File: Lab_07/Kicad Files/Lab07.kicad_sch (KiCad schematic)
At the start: 31 parts, among them J101 Conn_01x01_Socket, J102 Conn_01x01_Socket, J103 Conn_01x01_Socket, J104 Conn_01x01_Socket, J105 Conn_01x01_Pin, J106 Conn_01x01_Pin, J301 Conn_01x01_Socket, J302 Conn_01x01_Socket, J303 Conn_01x01_Socket, J304 Conn_01x01_Socket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

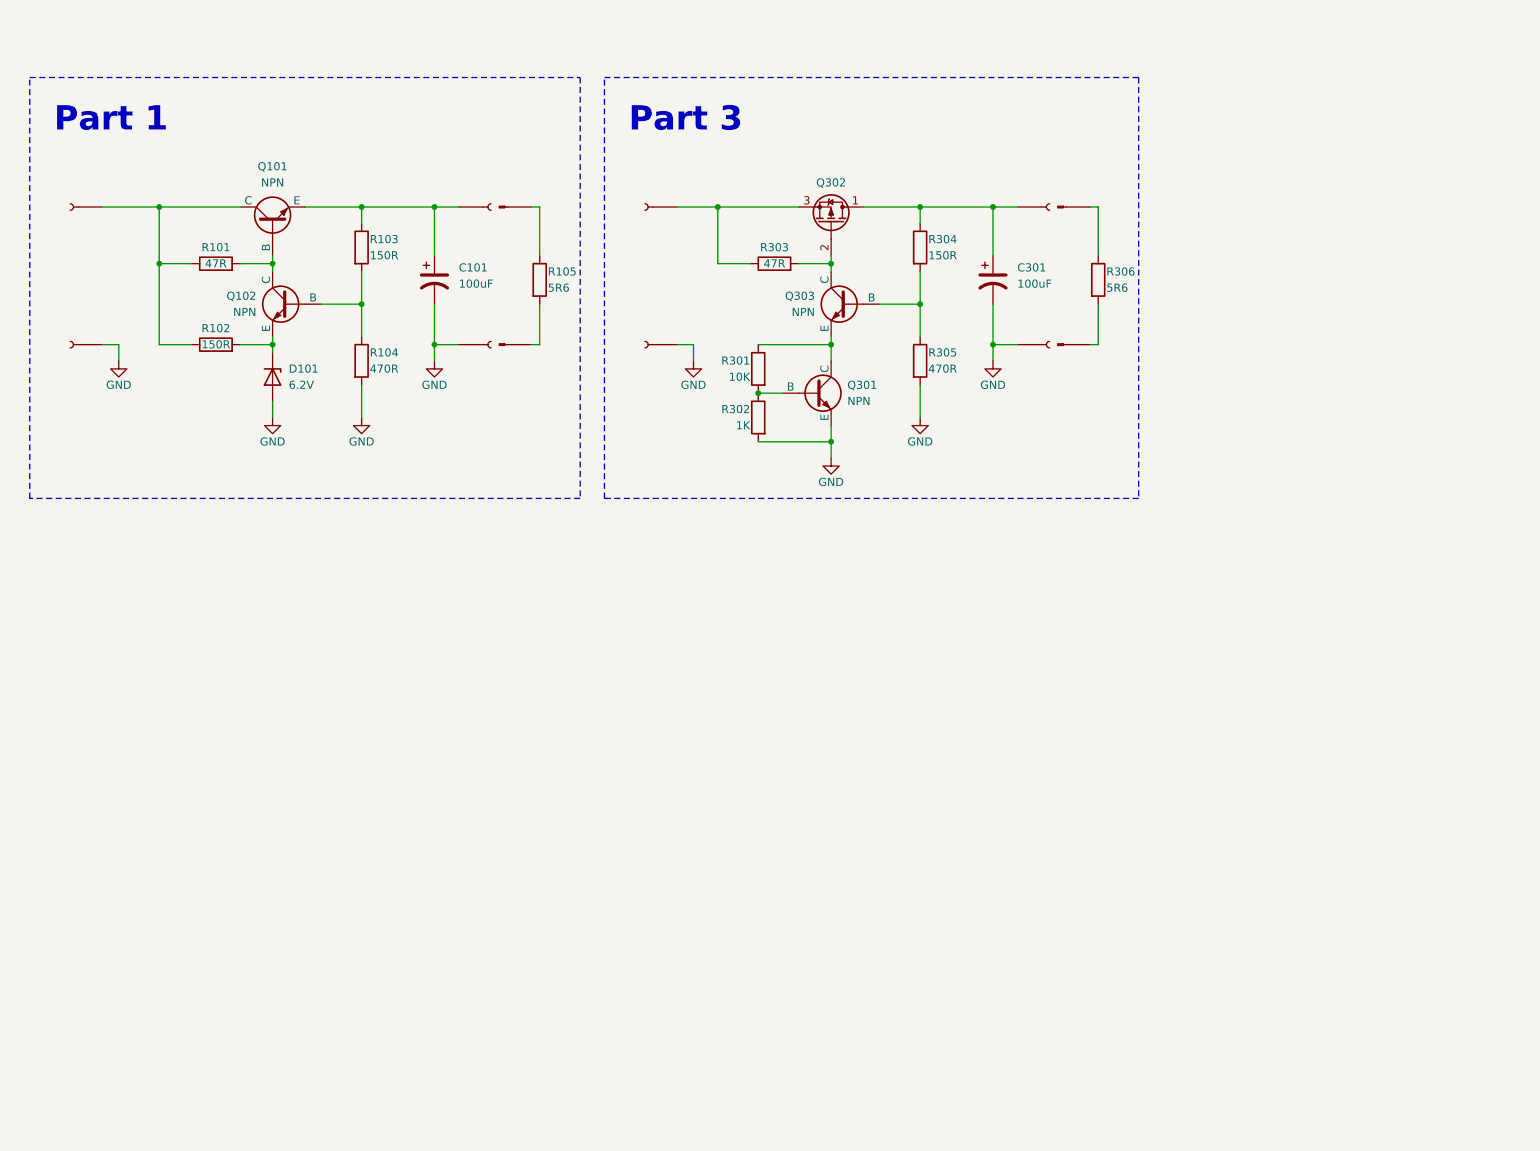
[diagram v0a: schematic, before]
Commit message: Revise Lab 7 Schematic
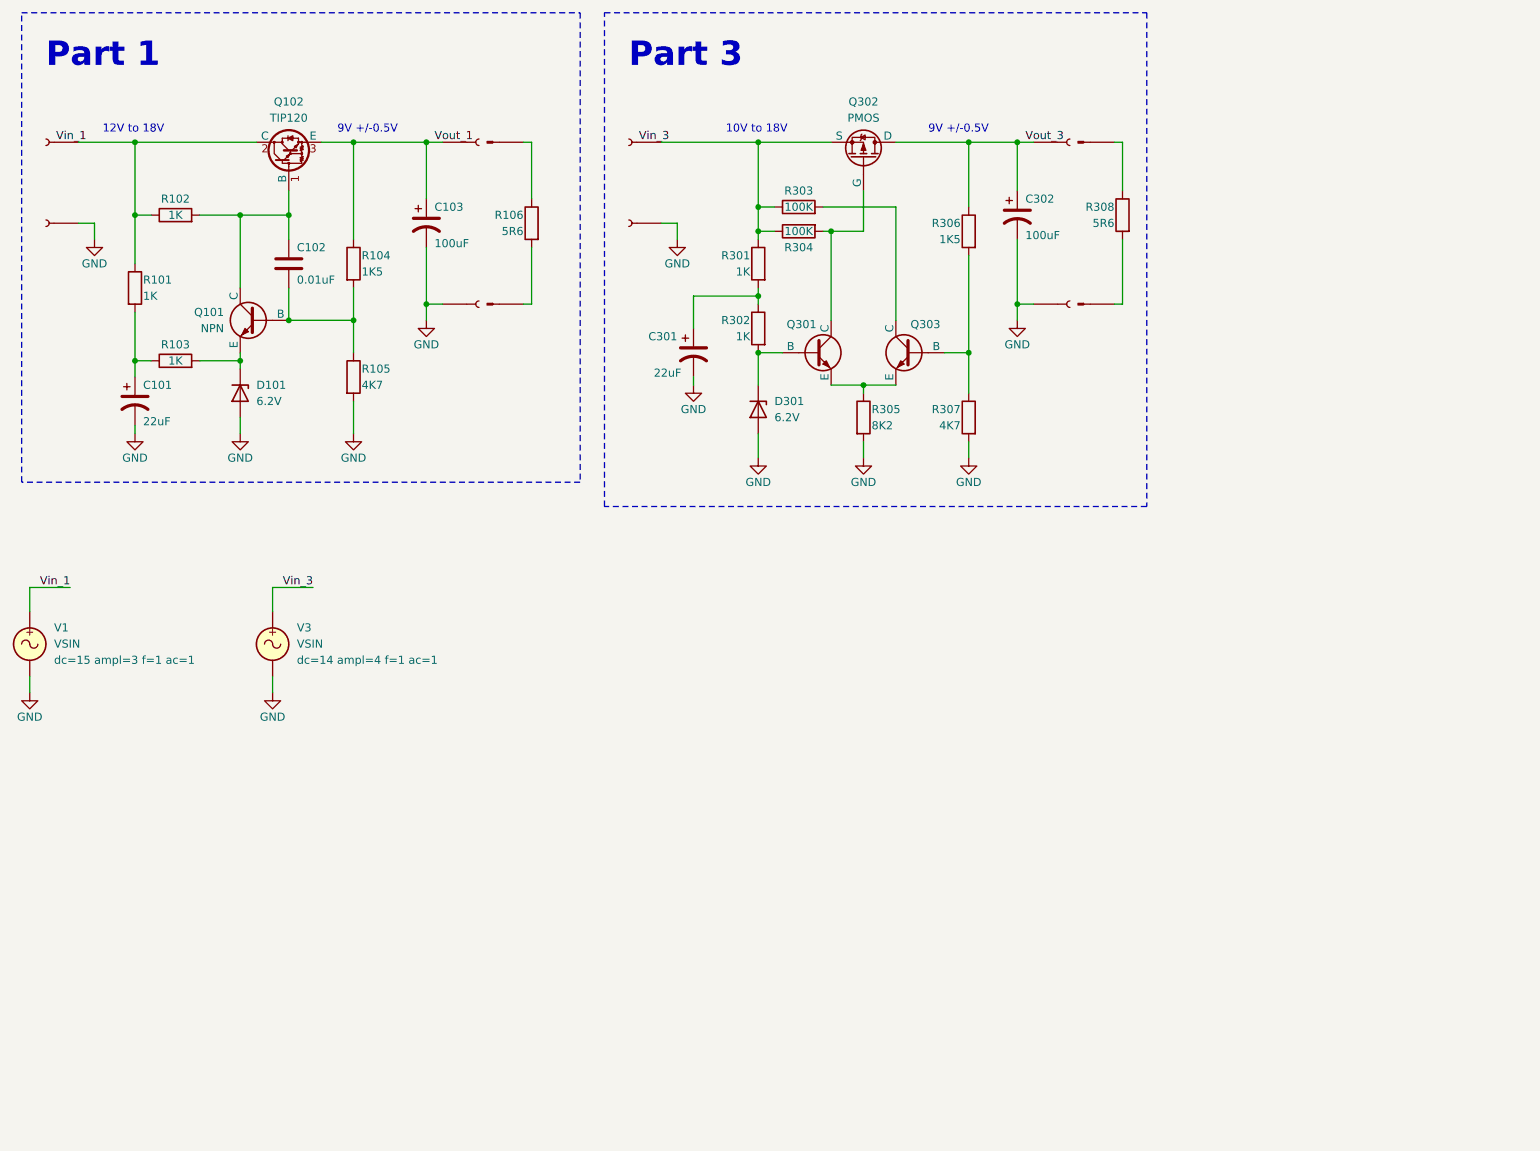
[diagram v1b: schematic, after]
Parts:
- removed J103, J104, J303, J304: Conn_01x01_Socket, symbol Connector:Conn_01x01_Socket
- removed J105, J106, J305, J306: Conn_01x01_Pin, symbol Connector:Conn_01x01_Pin
- removed Q101: NPN, symbol Simulation_SPICE:NPN
- removed R105: 5R6, symbol Device:R
- added C101, C301: 22uF, symbol Device:C_Polarized_US
- added C102: 0.01uF, symbol Device:C
- added D301: 6.2V, symbol Device:D_Zener
- added J103, J304: 0, symbol LarryLab:Output_Terminal
- added J104, J303: Output_Terminal, symbol LarryLab:Output_Terminal
- added Q102: TIP120, Package_TO_SOT_THT:TO-220-3_Vertical, symbol Transistor_BJT:TIP120
- added R102: 1K, symbol Device:R
- added R106: 5R6, symbol Device:R
- added R306: 1K5, symbol Device:R
- added R307: 4K7, symbol Device:R
- added V1, V3: VSIN, symbol Simulation_SPICE:VSIN
- Q302: value Q_PMOS_DGS -> PMOS
- R101: value 47R -> 1K
- R103: renamed from R102; value 150R -> 1K
- R104: renamed from R103; value 150R -> 1K5
- R105: renamed from R104; value 470R -> 4K7
- R301: value 10K -> 1K
- R303: value 47R -> 100K
- R304: value 150R -> 100K
- R305: value 470R -> 8K2
- renumbered C101 to C103, C301 to C302, Q102 to Q101, R306 to R308
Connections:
- net GND: now also C101.2, C301.2, D301.2 (A), J104.1 (In), J304.1 (In), R307.2, V1.2, V3.2; no longer Q301.3 (E), R302.2
- net at Q101.1 (C): now also C102.1, Q102.1 (B), R102.2; no longer R101.2
- net at Q101.2 (B), R104.2, R105.1: now also C102.2
- net Vin_1: now reaches J101.1 (Pin_1), R101.1
- net Vin_1: now also Q102.2 (C), R102.1, V1.1; no longer R103.1
- net Vout_1: now reaches C103.1, R104.1
- net Vout_1: now also J103.1 (In), Q102.3 (E)
- net Vout_3: now reaches C302.1, Q302.1 (D)
- net Vout_3: now also J303.1 (In), R306.1; no longer R304.1
- net at Q303.1 (C), R303.2: no longer Q302.2 (G)
- net Vin_3: now reaches J301.1 (Pin_1), Q302.3 (S), R303.1
- net Vin_3: now also R301.1, R304.1, V3.1
- net at R301.2, R302.1: now also C301.1; no longer Q301.2 (B)
- net at R308.1: now also J303.2 (Out)
- net at R308.2: now also J304.2 (Out)
- new net: C101.1, R101.2, R103.1
- new net: Q301.1 (C), Q302.2 (G), R304.2
- new net: Q303.2 (B), R306.2, R307.1
- new net: D301.1 (K), Q301.2 (B), R302.2
- new net: Q301.3 (E), Q303.3 (E), R305.1
- new net: J104.2 (Out), R106.2
- new net: J103.2 (Out), R106.1
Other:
- note added: "10V to 18V"
- note added: "12V to 18V"
- note added: "9V +/-0.5V"
- title: Linear Power Supplies -> Discrete Series Linear Voltage Regulators
- moved on the sheet: C103, C302, D101, Q101, Q302, R103, R104, R105, R303, R308

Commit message: Finish Lab 7
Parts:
- added Q103: NPN, Package_TO_SOT_THT:TO-92L_Inline_Wide, symbol Transistor_BJT:2N3904
- added R104: 390m, Resistor_THT:R_Axial_DIN0207_L6.3mm_D2.5mm_P2.54mm_Vertical, symbol Device:R
- C101, C103, C302: footprint (none) -> Capacitor_THT:CP_Radial_D10.0mm_P5.00mm
- C102: footprint (none) -> Capacitor_THT:C_Disc_D10.0mm_W2.5mm_P5.00mm
- C301: value 22uF -> 220uF; footprint (none) -> Capacitor_THT:CP_Radial_D10.0mm_P5.00mm
- D101, D301: footprint (none) -> Diode_THT:D_DO-41_SOD81_P7.62mm_Horizontal
- J101, J102, J103, J104, J301, J302, J303, J304: footprint (none) -> TestPoint:TestPoint_Loop_D2.54mm_Drill1.5mm_Beaded
- Q101, Q301, Q303: footprint (none) -> Package_TO_SOT_THT:TO-92L_Inline_Wide; symbol Simulation_SPICE:NPN -> Transistor_BJT:2N3904
- Q102: value TIP120 -> TIP102
- Q302: value PMOS -> IRF9Z24N; footprint (none) -> Package_TO_SOT_THT:TO-220-3_Vertical; symbol Device:Q_PMOS_DGS -> Device:Q_PMOS_GDS
- R101, R103, R301, R302, R303, R304, R305, R306, R307: footprint (none) -> Resistor_THT:R_Axial_DIN0207_L6.3mm_D2.5mm_P7.62mm_Horizontal
- R102: value 1K -> 2K2; footprint (none) -> Resistor_THT:R_Axial_DIN0207_L6.3mm_D2.5mm_P7.62mm_Horizontal
- R105: renamed from R104; value 1K5 -> 680R; footprint (none) -> Resistor_THT:R_Axial_DIN0207_L6.3mm_D2.5mm_P7.62mm_Horizontal
- R106: renamed from R105; value 4K7 -> 2K2; footprint (none) -> Resistor_THT:R_Axial_DIN0207_L6.3mm_D2.5mm_P7.62mm_Horizontal
- V1, V3: now left out of the parts list
- renumbered R106 to R107
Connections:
- net Vout_1: now also Q103.1 (E), R104.2; no longer Q102.3 (E)
- net Vout_3: now also Q302.2 (D); no longer Q302.1 (D)
- net at C102.1, Q102.1 (B), R102.2: now also Q101.3 (C), Q103.3 (C); no longer Q101.1 (C)
- net at D101.1 (K), R103.2: now also Q101.1 (E); no longer Q101.3 (E)
- net at R303.2: now also Q303.3 (C); no longer Q303.1 (C)
- new net: Q301.3 (C), Q302.1 (G), R304.2
- new net: Q102.3 (E), Q103.2 (B), R104.1
- new net: Q301.1 (E), Q303.1 (E), R305.1
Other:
- moved on the sheet: C101, C102, C103, C301, C302, D101, D301, Q302, R101, R102, R103, R105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

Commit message: Submit Labs 6 & 7
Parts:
- removed C102: 0.01uF, Capacitor_THT:C_Disc_D10.0mm_W2.5mm_P5.00mm, symbol Device:C
- added C401: 22uF, Capacitor_THT:CP_Radial_D10.0mm_P5.00mm, symbol Device:C_Polarized_US
- added C403: 100uF, Capacitor_THT:CP_Radial_D10.0mm_P5.00mm, symbol Device:C_Polarized_US
- added D401: 3.3V, Diode_THT:D_DO-41_SOD81_P7.62mm_Horizontal, symbol Device:D_Zener
- added J401, J402: Conn_01x01_Socket, TestPoint:TestPoint_Loop_D2.54mm_Drill1.5mm_Beaded, symbol Connector:Conn_01x01_Socket
- added J403: 0, TestPoint:TestPoint_Loop_D2.54mm_Drill1.5mm_Beaded, symbol LarryLab:Output_Terminal
- added J404: Output_Terminal, TestPoint:TestPoint_Loop_D2.54mm_Drill1.5mm_Beaded, symbol LarryLab:Output_Terminal
- added Q401, Q403: NPN, Package_TO_SOT_THT:TO-92L_Inline_Wide, symbol Transistor_BJT:2N3904
- added Q402: TIP102, Package_TO_SOT_THT:TO-220-3_Vertical, symbol Transistor_BJT:TIP120
- added R401, R403: 1K, Resistor_THT:R_Axial_DIN0207_L6.3mm_D2.5mm_P7.62mm_Horizontal, symbol Device:R
- added R402, R406: 2K2, Resistor_THT:R_Axial_DIN0207_L6.3mm_D2.5mm_P7.62mm_Horizontal, symbol Device:R
- added R404: 390m, Resistor_THT:R_Axial_DIN0207_L6.3mm_D2.5mm_P2.54mm_Vertical, symbol Device:R
- added R405: 680R, Resistor_THT:R_Axial_DIN0207_L6.3mm_D2.5mm_P7.62mm_Horizontal, symbol Device:R
- added R407: 5R6, symbol Device:R
- added RV401: 1K, symbol Device:R_Potentiometer
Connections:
- net GND: now also C401.2, C403.2, D401.2 (A), J402.1 (Pin_1), J404.1 (In), R406.2
- new net: J403.2 (Out), R407.1
- new net: J404.2 (Out), R407.2
- new net: R405.2, RV401.1
- new net: Q401.2 (B), RV401.2
- new net: R406.1, RV401.3
- new net: Q401.3 (C), Q402.1 (B), Q403.3 (C), R402.2
- new net: Q402.3 (E), Q403.2 (B), R404.1
- new net: D401.1 (K), Q401.1 (E), R403.2
- new net: C401.1, R401.2, R403.1
- new net Vin_4: J401.1 (Pin_1), Q402.2 (C), R401.1, R402.1
- new net Vout_4: C403.1, J403.1 (In), Q403.1 (E), R404.2, R405.1
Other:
- note added: "4V to 9V"
- note added: "Part 4"
- moved on the sheet: V1, V3
